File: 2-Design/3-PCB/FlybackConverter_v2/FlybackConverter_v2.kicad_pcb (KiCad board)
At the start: 2 copper layers, 125 x 40 mm, 52 parts, among them U1 TL431DBV, U2 LM7812_TO220

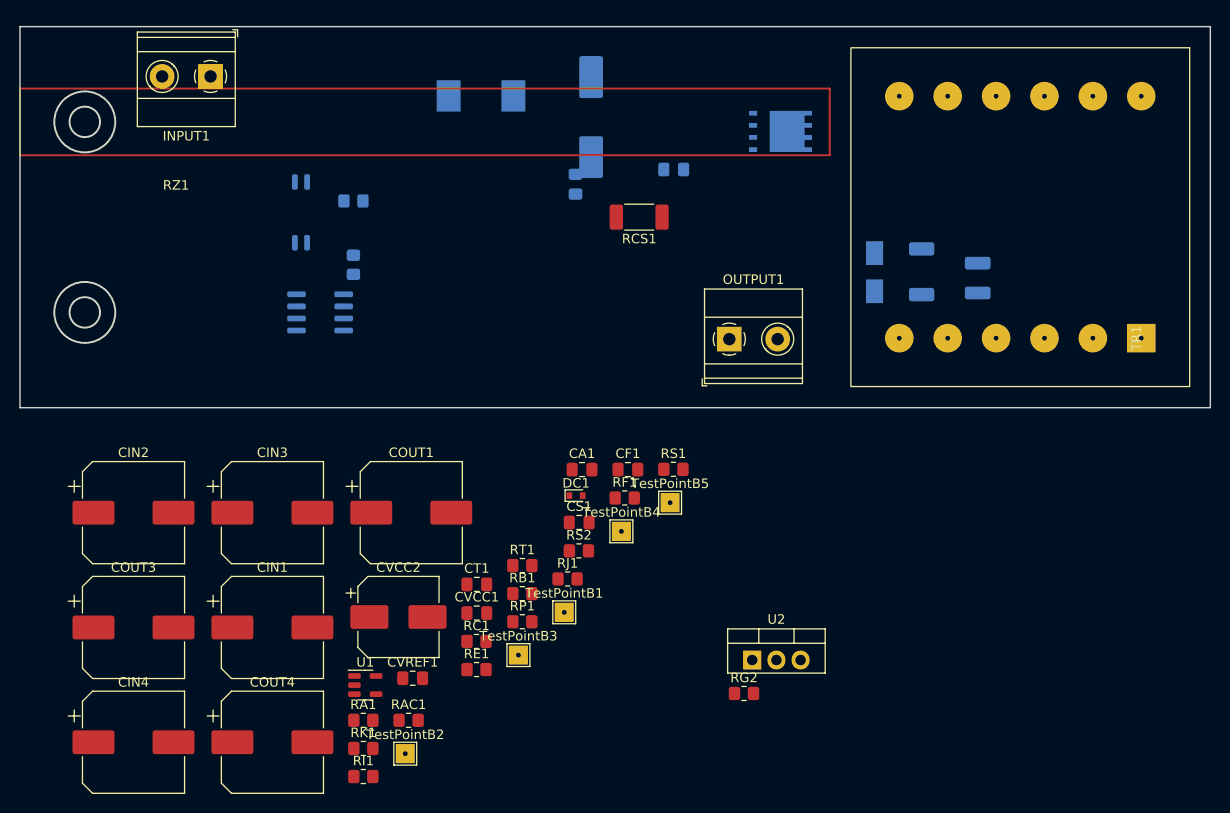
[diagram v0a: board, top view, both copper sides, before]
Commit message: FlybackConverter_v2 first placement done, gate loop is too long, positions will be updated blockwise.
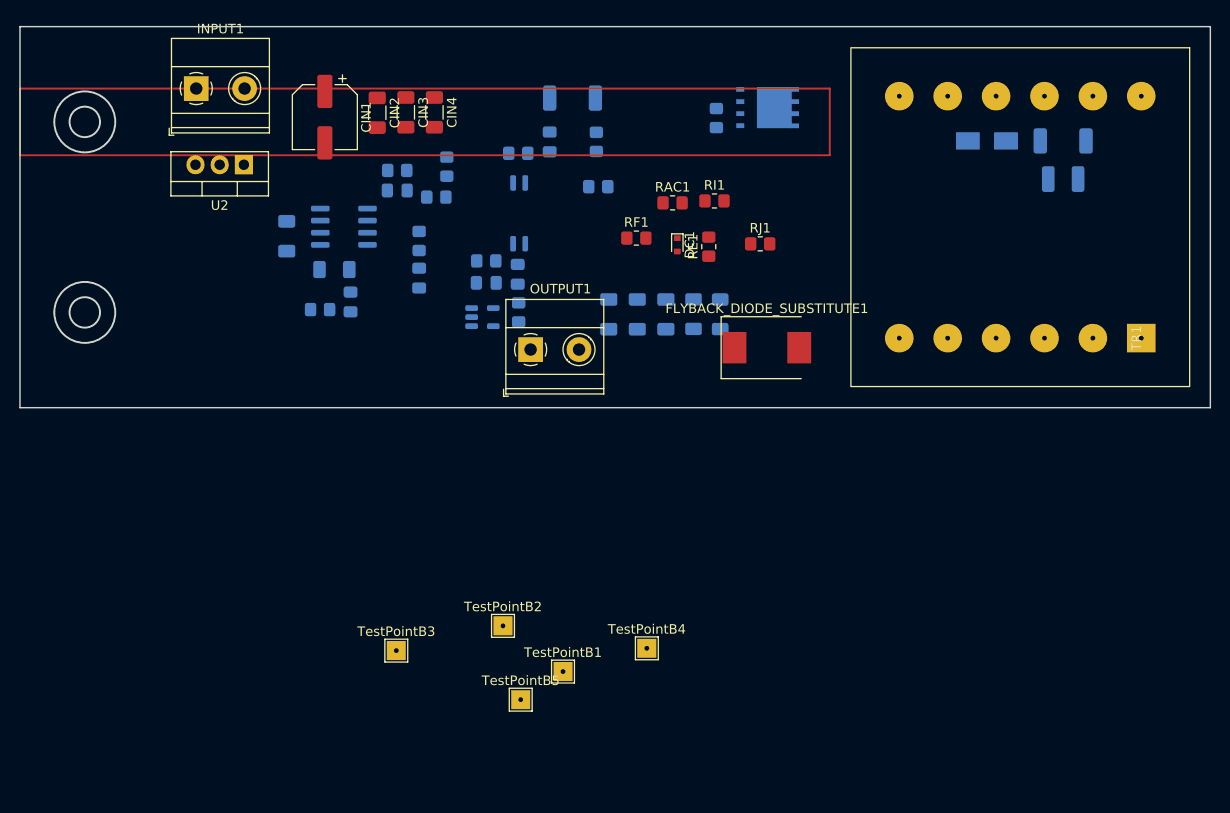
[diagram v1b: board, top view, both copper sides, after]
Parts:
- removed COUT4: C, Capacitor_SMD:CP_Elec_10x10.5
- removed CVCC2: C, Capacitor_SMD:CP_Elec_8x5.4
- added RLmin1: 4.7k, Resistor_SMD:R_1206_3216Metric_Pad1.30x1.75mm_HandSolder, B.Cu at (85.7, 45.2)
- added RLmin2: 4.7k, Resistor_SMD:R_1206_3216Metric_Pad1.30x1.75mm_HandSolder, B.Cu at (88.5, 45.2)
- CA1, CF1, CS1, CT1, RA1, RB1, RC1, RCS1, RG2, RK1, RP1, RS1, RS2, RT1, U1: moved to B.Cu
- CIN1: value C -> 47uF; footprint Capacitor_SMD:CP_Elec_10x10.5 -> Capacitor_SMD:CP_Elec_6.3x7.7
- CIN2, CIN3: value C -> 10uF; footprint Capacitor_SMD:CP_Elec_10x10.5 -> Capacitor_SMD:C_1206_3216Metric_Pad1.33x1.80mm_HandSolder
- CIN4: value C -> 100nF; footprint Capacitor_SMD:CP_Elec_10x10.5 -> Capacitor_SMD:C_1206_3216Metric_Pad1.33x1.80mm_HandSolder
- COUT1: value C -> 10uF; footprint Capacitor_SMD:CP_Elec_10x10.5 -> Capacitor_SMD:C_1206_3216Metric_Pad1.33x1.80mm_HandSolder; moved to B.Cu
- COUT2: value C -> 2.2uF; footprint Capacitor_SMD:CP_Elec_10x10.5 -> Capacitor_SMD:C_1206_3216Metric_Pad1.33x1.80mm_HandSolder
- COUT3: value C -> 100nF; footprint Capacitor_SMD:CP_Elec_10x10.5 -> Capacitor_SMD:C_1206_3216Metric_Pad1.33x1.80mm_HandSolder; moved to B.Cu
- CVCC1, CVREF1: value C -> 1uF; footprint Capacitor_SMD:C_0805_2012Metric_Pad1.18x1.45mm_HandSolder -> Capacitor_SMD:C_1206_3216Metric_Pad1.33x1.80mm_HandSolder; moved to B.Cu
- FLYBACK_DIODE_SUBSTITUTE1: moved to F.Cu
- moved U2 74.5 mm to (38.5, 29.5), turned to 180 degrees
- moved CIN4 73.3 mm to (58.5, 24.0), turned to -90 degrees
- moved RI1 70.8 mm to (87.9, 33.3)
- moved COUT3 64.8 mm to (82.8, 45.2), turned to -90 degrees
- moved RAC1 61.0 mm to (83.5, 33.5)
- moved RG2 60.5 mm to (88.1, 24.6), turned to 90 degrees
- moved RA1 57.8 mm to (54.6, 30.1), turned to 180 degrees
- moved CIN1 53.9 mm to (47.0, 24.5), turned to -90 degrees
- moved RE1 50.6 mm to (87.3, 38.1), turned to 90 degrees
- moved RC1 49.9 mm to (59.8, 29.7), turned to 90 degrees
- moved RP1 49.2 mm to (67.3, 28.3)
- moved CIN2 49.2 mm to (52.5, 24.0), turned to -90 degrees
- moved RK1 48.6 mm to (67.3, 45.0), turned to -90 degrees
- moved CVCC1 44.3 mm to (43.0, 37.0), turned to 90 degrees
- moved CIN3 44.3 mm to (55.5, 24.0), turned to -90 degrees
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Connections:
- OUTPUT1 pad 1: Net-(COUT1-Pad1) -> GND1
- OUTPUT1 pad 2: GND1 -> Net-(COUT1-Pad1)
- TR1 pad 1: Net-(DSnubber1-Pad2) -> (no net)
- TR1 pad 11: (no net) -> Net-(CIN1-Pad1)
- TR1 pad 2: (no net) -> Net-(FLYBACK_DIODE_SUBSTITUTE1-Pad2)
- TR1 pad 3: Net-(CIN1-Pad1) -> (no net)
- TR1 pad 4: Net-(FLYBACK_DIODE_SUBSTITUTE1-Pad2) -> (no net)
- TR1 pad 5: (no net) -> GND1
- TR1 pad 6: GND1 -> (no net)
- TR1 pad 8: (no net) -> Net-(DSnubber1-Pad2)

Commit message: FlybackConverter_v2 layout updated. RJ1, 7812, and (maybe) gate driver via problematic.
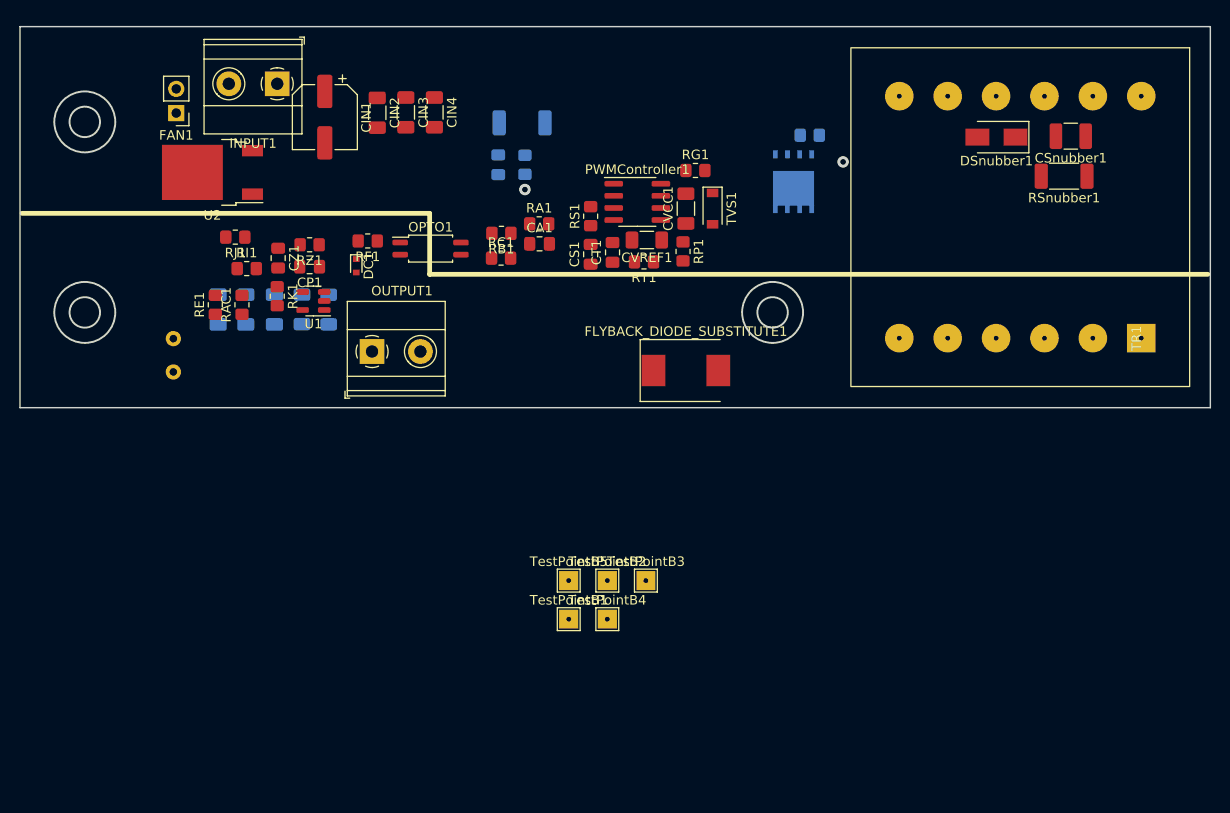
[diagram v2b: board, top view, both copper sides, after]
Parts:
- added COUT2: 10uF, Capacitor_SMD:C_1206_3216Metric_Pad1.33x1.80mm_HandSolder, B.Cu at (35.8, 44.7)
- added FAN1: Conn_01x02_Female, Connector_PinHeader_2.54mm:PinHeader_1x02_P2.54mm_Vertical, F.Cu at (31.4, 24.1)
- added TVS1: MBRA340, Diode_SMD:D_SOD-123, F.Cu at (87.7, 34.1)
- CA1, CP1, CS1, CSnubber1, CT1, CVCC1, CVREF1, CZ1, DSnubber1, OPTO1, PWMController1, RA1, RB1, RC1, RG1, RK1, RP1, RS1, RSnubber1, RT1, RZ1, U1: moved to F.Cu
- COUT1: value 10uF -> 100uF; footprint Capacitor_SMD:C_1206_3216Metric_Pad1.33x1.80mm_HandSolder -> Capacitor_THT:C_Radial_D8.0mm_H11.5mm_P3.50mm
- U2: footprint Package_TO_SOT_THT:TO-220-3_Vertical -> Package_TO_SOT_SMD:TO-252-2
- moved RJ1 55.1 mm to (37.6, 37.1), turned to 180 degrees
- moved RE1 52.2 mm to (35.5, 44.2)
- moved RI1 49.6 mm to (38.8, 40.4)
- moved RAC1 46.4 mm to (38.3, 44.2), turned to 90 degrees
- moved COUT1 45.8 mm to (31.1, 47.8)
- moved CVCC1 42.0 mm to (84.9, 34.1)
- moved RLmin1 41.1 mm to (44.6, 44.7)
- moved RLmin2 41.1 mm to (47.4, 44.7)
- moved COUT3 41.1 mm to (38.7, 44.7)
- moved COUT4 41.1 mm to (41.7, 44.7)
- moved RT1 34.4 mm to (80.5, 39.7), turned to 180 degrees
- moved DC1 33.8 mm to (50.3, 40.1)
- moved CVREF1 32.9 mm to (80.8, 37.4), turned to 180 degrees
- moved PWMController1 30.9 mm to (79.8, 33.4), turned to 0 degrees
- moved RF1 28.2 mm to (51.5, 37.5), turned to 180 degrees
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- renumbered COUT2 to COUT3, COUT3 to COUT4
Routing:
- net Net-(MOSFET1-Pad4): vias 0 -> 1
- net Net-(CF1-Pad1): vias 0 -> 1
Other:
- outline, holes or cut-outs redrawn

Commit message: Small updates on schematic and layout.
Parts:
- COUT1: value 100uF -> 47uF; footprint Capacitor_THT:C_Radial_D8.0mm_H11.5mm_P3.50mm -> Capacitor_SMD:CP_Elec_10x12.6; moved to F.Cu
- COUT2: value 10uF -> 2.2uF; footprint Capacitor_SMD:C_1206_3216Metric_Pad1.33x1.80mm_HandSolder -> Capacitor_SMD:C_1210_3225Metric_Pad1.33x2.70mm_HandSolder
- COUT3, COUT4: footprint Capacitor_SMD:C_1206_3216Metric_Pad1.33x1.80mm_HandSolder -> Capacitor_SMD:C_1210_3225Metric_Pad1.33x2.70mm_HandSolder
- moved COUT4 29.3 mm to (70.9, 46.8)
- moved RLmin1 29.3 mm to (73.8, 46.8)
- moved RLmin2 29.3 mm to (76.6, 46.8)
- moved COUT3 28.8 mm to (67.4, 46.8)
- moved COUT2 28.0 mm to (63.7, 46.8)
- moved DC1 16.8 mm to (33.5, 39.2)
- moved MOSFET1 12.6 mm to (96.6, 18.8), turned to 90 degrees
- moved RS2 10.9 mm to (78.7, 27.2)
- moved CF1 10.9 mm to (75.8, 26.9)
- moved RCS1 10.8 mm to (78.1, 22.1)
- moved CA1 10.1 mm to (79.6, 37.7)
- moved CVREF1 10.1 mm to (90.9, 37.3)
- moved PWMController1 10.1 mm to (89.9, 33.3)
- moved RB1 10.1 mm to (75.6, 36.6)
- moved RP1 10.1 mm to (94.7, 38.5)
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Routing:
- net Net-(CIN1-Pad1): vias 0 -> 1

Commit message: Small updates & 3D models added, tracks to be placed.
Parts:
- added REF**: 40x20_Heatsink, kutup:40x20_Heatsink, F.Cu at (55.0, 35.0)
- CF1, COUT2, COUT3, COUT4, RLmin1, RLmin2, RS2: moved to F.Cu
- INPUT1, OUTPUT1: footprint TerminalBlock_Phoenix:TerminalBlock_Phoenix_MKDS-1,5-2-5.08_1x02_P5.08mm_Horizontal -> kutup:sevgi_konnektosu
- moved TestPointB2 45.3 mm to (80.5, 28.0)
- moved TestPointB5 41.1 mm to (45.7, 42.1)
- moved TestPointB1 40.8 mm to (69.5, 36.5)
- moved TestPointB3 38.4 mm to (59.0, 41.5)
- moved COUT1 37.4 mm to (67.3, 47.2), turned to 90 degrees
- moved RLmin1 31.1 mm to (42.7, 47.6), turned to 90 degrees
- moved RLmin2 31.1 mm to (45.5, 47.5), turned to 90 degrees
- moved TestPointB4 30.2 mm to (92.5, 51.5)
- moved OUTPUT1 13.7 mm to (39.8, 55.5)
- moved COUT2 11.7 mm to (52.0, 47.6), turned to 90 degrees
- moved COUT3 11.7 mm to (55.7, 47.6), turned to 90 degrees
- moved COUT4 11.7 mm to (59.2, 47.6), turned to 90 degrees
- moved INPUT1 9.68 mm to (30.8, 14.6), turned to 180 degrees
- moved CIN4 8.45 mm to (53.4, 27.3), turned to 90 degrees
- moved DC1 8.08 mm to (41.2, 36.8), turned to 180 degrees
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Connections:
- net GND1 renamed GNDREF
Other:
- board size 125 x 40 mm -> 120 x 40 mm

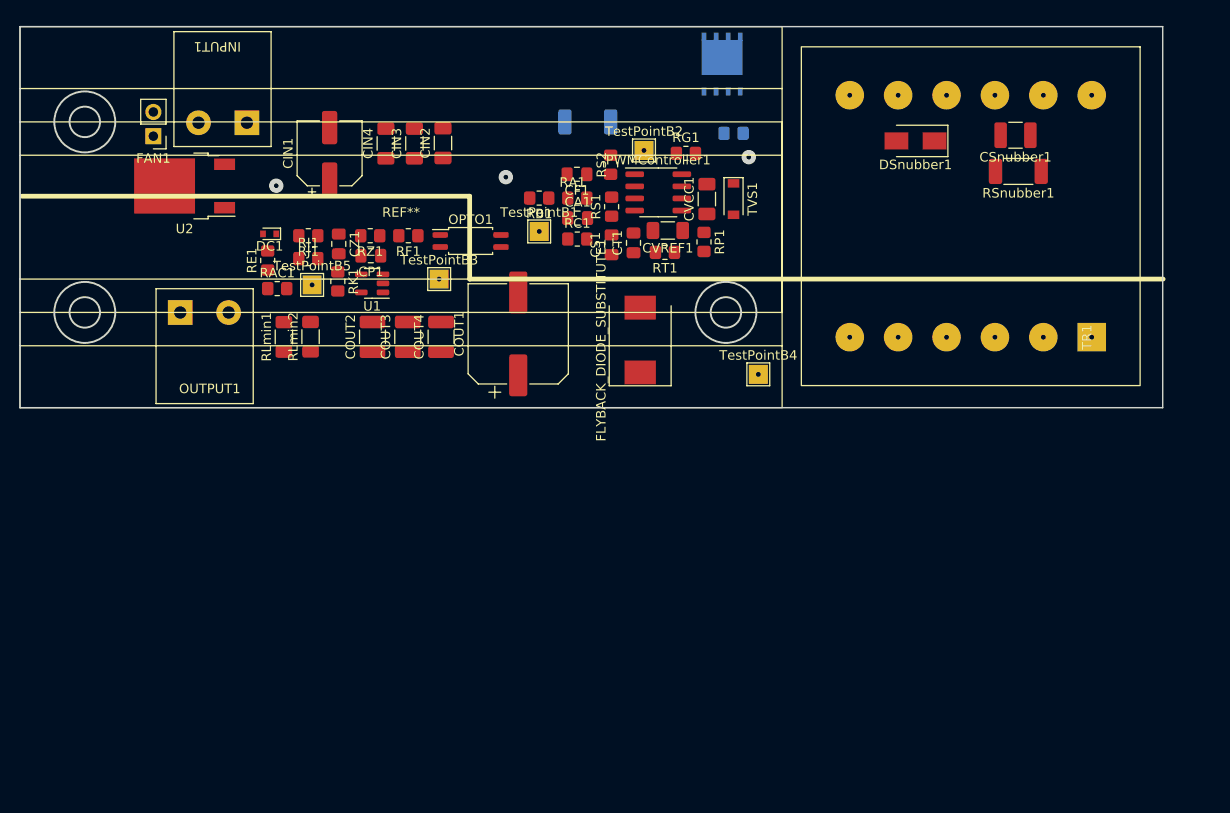
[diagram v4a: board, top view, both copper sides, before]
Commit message: Tracks around the damn IC are almost done.
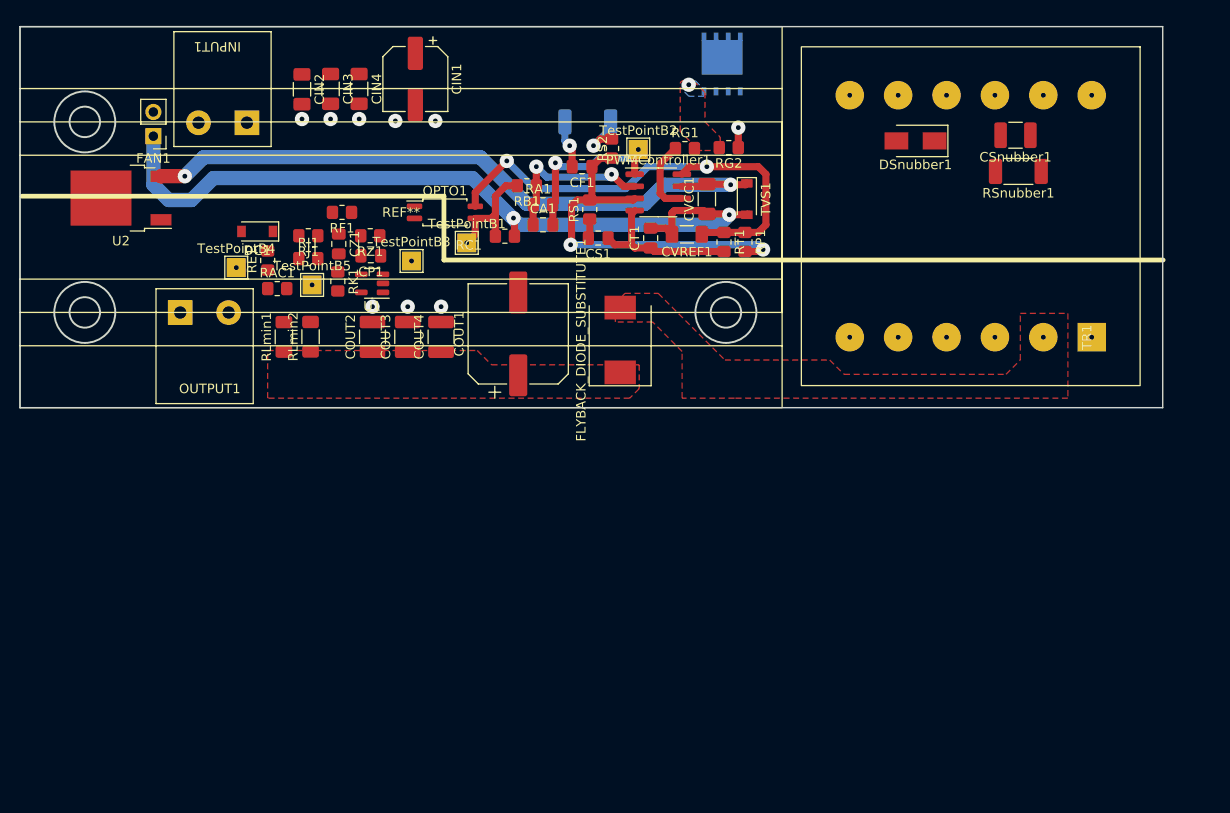
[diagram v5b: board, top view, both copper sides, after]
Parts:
- DC1: footprint Diode_SMD:D_SOD-523 -> Diode_SMD:D_SOD-123
- RG2: moved to F.Cu
- moved TestPointB4 55.9 mm to (37.7, 40.3)
- moved CIN2 15.8 mm to (44.6, 21.6), turned to -90 degrees
- moved CIN1 11.9 mm to (56.5, 20.5), turned to -90 degrees
- moved CIN3 10.5 mm to (47.6, 21.5), turned to -90 degrees
- moved TestPointB1 7.69 mm to (61.9, 37.7)
- moved RC1 7.61 mm to (65.9, 37.0)
- moved RF1 7.38 mm to (48.8, 34.5)
- moved U2 6.80 mm to (25.6, 33.0)
- moved CIN4 6.37 mm to (50.6, 21.5), turned to -90 degrees
- moved RT1 6.30 mm to (88.9, 37.6), turned to -90 degrees
- moved RP1 4.30 mm to (91.1, 37.6)
- moved OPTO1 4.04 mm to (59.6, 34.5)
- moved CA1 3.70 mm to (69.9, 35.8)
- moved RA1 3.67 mm to (69.9, 33.7)
- moved TestPointB3 3.47 mm to (56.1, 39.6)
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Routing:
- net GND: track 0.00 -> 89.7 mm, vias 0 -> 8
- net Net-(CVCC1-Pad2): track 0.00 -> 70.5 mm, vias 0 -> 2
- net Net-(CVREF1-Pad1): track 0.00 -> 51.2 mm, vias 0 -> 2
- net Net-(CF1-Pad1): track 0.00 -> 39.8 mm, vias 1 -> 2
- net Net-(CA1-Pad2): track 0.00 -> 19.0 mm, vias 0 -> 1
- net Net-(CA1-Pad1): track 0.00 -> 17.7 mm, vias 0 -> 2
- net Net-(CS1-Pad1): track 0.00 -> 16.5 mm
- net Net-(OPTO1-Pad3): track 0.00 -> 12.8 mm
- net Net-(PWMController1-Pad6): track 0.00 -> 7.86 mm
- net Net-(MOSFET1-Pad1): track 0.00 -> 7.54 mm, vias 0 -> 2
- net Net-(CS1-Pad2): track 0.00 -> 2.06 mm
- net Net-(CIN1-Pad1): vias 1 -> 0
- net GNDREF: vias 0 -> 3
- added copper zone on F.Cu, net Net-(COUT1-Pad1)
- added copper zone on F.Cu, net Net-(FLYBACK_DIODE_SUBSTITUTE1-Pad2)
- added copper zone on B.Cu, net Net-(MOSFET1-Pad4)
- added copper zone on F.Cu, net Net-(MOSFET1-Pad4)

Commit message: Output side tracks almost completed.,
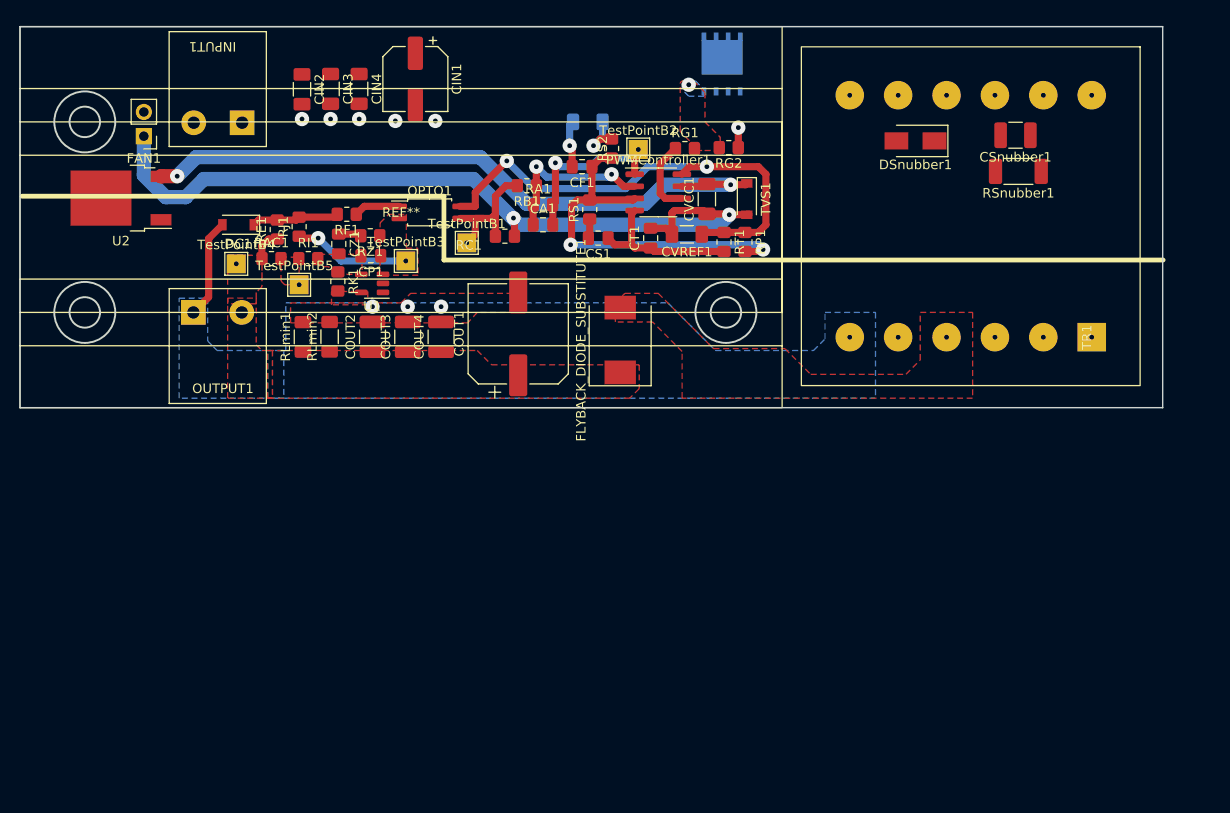
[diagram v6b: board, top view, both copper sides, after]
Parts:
- RCS1: footprint Resistor_SMD:R_2010_5025Metric_Pad1.40x2.65mm_HandSolder -> Resistor_SMD:R_1206_3216Metric_Pad1.30x1.75mm_HandSolder
- moved RE1 3.40 mm to (42.0, 36.3)
- moved RAC1 3.21 mm to (41.4, 39.4)
- moved DC1 2.12 mm to (37.9, 35.8)
- moved RLmin1 2.00 mm to (44.7, 47.6)
- moved RLmin2 2.00 mm to (47.5, 47.5)
- moved OPTO1 1.60 mm to (58.0, 34.5)
- moved OUTPUT1 1.38 mm to (41.2, 55.5)
- moved TestPointB5 1.36 mm to (44.3, 42.1)
- moved RJ1 1.35 mm to (44.3, 36.0), turned to 90 degrees
- moved FAN1 1.00 mm to (28.0, 26.5)
- moved TestPointB3 0.60 mm to (55.5, 39.6)
- moved RF1 0.54 mm to (49.3, 34.7)
- moved INPUT1 0.50 mm to (30.3, 14.6)
- moved TestPointB4 0.40 mm to (37.7, 39.9)
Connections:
- TR1 pad 2: Net-(FLYBACK_DIODE_SUBSTITUTE1-Pad2) -> (no net)
- TR1 pad 4: (no net) -> Net-(FLYBACK_DIODE_SUBSTITUTE1-Pad2)
- TR1 pad 5: GNDREF -> (no net)
- TR1 pad 6: (no net) -> GNDREF
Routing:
- net Net-(CP1-Pad1): track 0.00 -> 12.8 mm, vias 0 -> 1
- net GNDREF: track 0.00 -> 10.5 mm
- net Net-(DC1-Pad1): track 0.00 -> 9.21 mm
- net Net-(OPTO1-Pad1): track 0.00 -> 4.86 mm
- net Net-(COUT1-Pad1): track 0.00 -> 3.24 mm
- net Net-(OPTO1-Pad3): track 12.8 -> 15.3 mm
- net Net-(CZ1-Pad1): track 0.00 -> 2.37 mm
- net Net-(CVREF1-Pad1): track 51.2 -> 52.8 mm
- added copper zone on B.Cu, net GNDREF
- added copper zone on F.Cu, net GNDREF
- added copper zone on F.Cu, net Net-(CP1-Pad1)
- added copper zone on F.Cu, net Net-(CP1-Pad2)
- added copper zone on F.Cu, net Net-(RAC1-Pad2)
